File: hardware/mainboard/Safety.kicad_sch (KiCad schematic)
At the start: 19 parts, among them K1 IMB03ITS, Q6 2N7002, Q8 2N7002, Q9 2N7002, U3 74AUP1G32

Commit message: schematic?
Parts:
- removed C58: 100nF, Capacitor_SMD:C_0603_1608Metric, symbol Device:C_Small
- removed K1: IMB03ITS, Samacsys:IMB03ITS, symbol Samacsys_kicad_sym:IMB03ITS
- removed R15, R32, R41: 100, Resistor_SMD:R_0603_1608Metric, symbol Device:R_Small
- added K1: IM07DTS, Samacsys:IM23TS, symbol Samacsys_kicad_sym:IM07DTS
- added R38: 1k, Resistor_SMD:R_0603_1608Metric, symbol Device:R_Small
- added TP1, TP4: TestPoint_Small, TestPoint:TestPoint_Pad_D1.0mm, symbol Connector:TestPoint_Small
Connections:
- net AMS_OK is gone; now on net LED_ERR: Q9.1 (G), R13.1
- net WEB is gone; now on net WTDG_ERROR: Q8.1 (G)
- net GND: now also TP4.1
- net RELAY-: now also K1.8 (COIL_2)
- net SAFETY_IN: now also K1.3 (COM_1)
- net SAFETY_OUT: now also K1.4 (NO_1)
- net WTDG_ERROR: now also R38.1; no longer R14.2, U3.2
- net +3.3V renamed +3.3VIO
- net +5V renamed +24V
- net +24V: now also K1.1 (COIL_1)
- new net: R14.2, R38.2, TP1.1, U3.2
- no-connect marks 0 -> 4
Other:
- moved on the sheet: D7, Q8, Q9, R13, R14, TP17, TP18

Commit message: sync
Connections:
- net LED_ERR is gone; now on net WTDG_ERROR: Q8.3 (D), Q9.1 (G), R13.1
- net WTDG_ERROR: no longer Q8.1 (G), R38.1, U3.4
- new net LATCHERR: Q8.1 (G), R38.1, U3.4
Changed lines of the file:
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@@
 	(wire
 		(pts
-			(xy 125.73 133.35) (xy 147.32 133.35)
+			(xy 125.73 133.35) (xy 176.53 133.35)
 		)
 		(stroke
@@
 		)
 	)
+	(wire
+		(pts
+			(xy 176.53 133.35) (xy 176.53 82.55)
+		)
+		(stroke
+			(width 0)
+			(type default)
+		)
+	)
 	(polyline
 		(pts
@@
 	(wire
 		(pts
-			(xy 91.44 82.55) (xy 93.98 82.55)
+			(xy 91.44 82.55) (xy 176.53 82.55)
 		)
 		(stroke
@@
 			(width 0)
 			(type default)
+		)
+	)
+	(label "LATCHERR"
+		(at 127 133.35 0)
+		(effects
+			(font
+				(size 0.508 0.508)
+			)
+			(justify left bottom)
 		)
 	)
@@
 		)
 	)
-	(hierarchical_label "WTDG_ERROR"
-		(shape output)
-		(at 147.32 133.35 0)
+	(hierarchical_label "SAFETY_IN"
+		(shape bidirectional)
+		(at 118.11 45.72 0)
 		(effects
 			(font
@@
 		)
 	)
-	(hierarchical_label "LED_ERR"
-		(shape input)
-		(at 86.36 72.39 0)
-		(effects
-			(font
-				(size 1.27 1.27)
-			)
-			(justify left)
-		)
-	)
-	(hierarchical_label "SAFETY_IN"
-		(shape bidirectional)
-		(at 118.11 45.72 0)
-		(effects
-			(font
-				(size 1.27 1.27)
-			)
-			(justify left)
-		)
-	)
 	(hierarchical_label "AMS_ERROR"
 		(shape input)
@@
 	(hierarchical_label "WTDG_ERROR"
 		(shape output)
-		(at 93.98 82.55 0)
-		(effects
-			(font
+		(at 86.36 72.39 0)
+		(effects
+			(font

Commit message: hardware routing done, only touch ups will be needed if the board is aproved
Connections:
- net +3.3VIO renamed +5VIO
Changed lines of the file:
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@@
 	)
 	(symbol
-		(lib_id "power:+3.3V")
+		(lib_name "+5V_2")
+		(lib_id "power:+5V")
 		(at 99.06 67.31 270)
 		(unit 1)
@@
 		(on_board yes)
 		(dnp no)
-		(property "Reference" "#PWR059"
+		(property "Reference" "#PWR0119"
 			(at 95.25 67.31 0)
 			(effects
@@
 			)
 		)
-		(property "Value" "+3.3VIO"
+		(property "Value" "+5VIO"
 			(at 105.41 67.31 90)
 			(effects
@@
 			(project "PUTM_EV_AMS_MASTER_2025"
 				(path "/b456cffc-d9d7-4c91-91f2-36ec9a65dd1b/6eb4a2b1-8e5b-451b-b593-8aaaa3a4213e"
-					(reference "#PWR059")
+					(reference "#PWR0119")
 					(unit 1)
 				)
@@
 	)
 	(symbol
-		(lib_id "power:+3.3V")
-		(at 118.11 119.38 0)
-		(unit 1)
-		(exclude_from_sim no)
-		(in_bom yes)
-		(on_board yes)
-		(dnp no)
-		(property "Reference" "#PWR039"
-			(at 118.11 123.19 0)
-			(effects
-				(font
-					(size 1.27 1.27)
-				)
-				(hide yes)
-			)
-		)
-		(property "Value" "+3.3VIO"
-			(at 118.491 114.9858 0)
-			(effects
-				(font
-					(size 1.27 1.27)
-				)
-			)
-		)
-		(property "Footprint" ""
-			(at 118.11 119.38 0)
-			(effects
-				(font
-					(size 1.27 1.27)
-				)
-				(hide yes)
-			)
-		)
-		(property "Datasheet" ""
-			(at 118.11 119.38 0)
-			(effects
-				(font
-					(size 1.27 1.27)
-				)
-				(hide yes)
-			)
-		)
-		(property "Description" ""
-			(at 118.11 119.38 0)
-			(effects
-				(font
-					(size 1.27 1.27)
-				)
-				(hide yes)
-			)
-		)
-		(pin "1"
-		)
-		(instances
-			(project "PUTM_EV_BMS_HV_MASTER_2023"
-				(path "/b456cffc-d9d7-4c91-91f2-36ec9a65dd1b/6eb4a2b1-8e5b-451b-b593-8aaaa3a4213e"
-					(reference "#PWR039")
-					(unit 1)
-				)
-			)
-		)
-	)
-	(symbol
 		(lib_id "Device:R_Small")
 		(at 105.41 146.05 180)
@@
 	)
 	(symbol
-		(lib_id "power:+3.3V")
+		(lib_name "+5V_2")
+		(lib_id "power:+5V")
 		(at 74.93 121.92 0)
 		(unit 1)
@@
 		(on_board yes)
 		(dnp no)
-		(property "Reference" "#PWR044"
+		(property "Reference" "#PWR0121"
 			(at 74.93 125.73 0)
 			(effects
@@
 			)
 		)
-		(property "Value" "+3.3VIO"
-			(at 75.311 117.5258 0)
+		(property "Value" "+5VIO"
+			(at 74.93 118.11 0)
 			(effects
 				(font
@@
 		)
 		(instances
-			(project "PUTM_EV_BMS_HV_MASTER_2023"
+			(project "PUTM_EV_AMS_MASTER_2025"
 				(path "/b456cffc-d9d7-4c91-91f2-36ec9a65dd1b/6eb4a2b1-8e5b-451b-b593-8aaaa3a4213e"
-					(reference "#PWR044")
+					(reference "#PWR0121")
 					(unit 1)
 				)
+			)
+		)
+	)
+	(symbol
+		(lib_name "+5V_2")
+		(lib_id "power:+5V")
+		(at 118.11 119.38 0)
+		(unit 1)
+		(exclude_from_sim no)
+		(in_bom yes)
+		(on_board yes)
+		(dnp no)
+		(property "Reference" "#PWR0120"
+			(at 118.11 123.19 0)
+			(effects
+				(font
+					(size 1.27 1.27)
+				)
+				(hide yes)
+			)
+		)
+		(property "Value" "+5VIO"
+			(at 118.11 115.57 0)
+			(effects
+				(font
+					(size 1.27 1.27)
+				)
+			)
+		)
+		(property "Footprint" ""
+			(at 118.11 119.38 0)
+			(effects
+				(font
+					(size 1.27 1.27)
+				)
+				(hide yes)
+			)
+		)
+		(property "Datasheet" ""
+			(at 118.11 119.38 0)
+			(effects
+				(font
+					(size 1.27 1.27)
+				)
+				(hide yes)
+			)
+		)
+		(property "Description" ""
+			(at 118.11 119.38 0)
+			(effects
+				(font
+					(size 1.27 1.27)
+				)
+				(hide yes)
+			)
+		)
+		(pin "1"
+		)
+		(instances
+			(project "PUTM_EV_AMS_MASTER_2025"
+				(path "/b456cffc-d9d7-4c91-91f2-36ec9a65dd1b/6eb4a2b1-8e5b-451b-b593-8aaaa3a4213e"
+					(reference "#PWR0120")
+					(unit 1)
+				)

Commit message: isolation with every thing
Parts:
- removed D7: 60V/0.5/3A, Diode_SMD:D_SOD-123, symbol Device:D_Schottky_Small
- removed K1: IM07DTS, Samacsys:IM23TS, symbol Samacsys_kicad_sym:IM07DTS
- removed TP17, TP18: TestPoint_Small, TestPoint:TestPoint_THTPad_D1.0mm_Drill0.5mm, symbol Connector:TestPoint_Small
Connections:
- net RELAY- renamed ERROR_RELAY-
- no-connect marks 4 -> 0

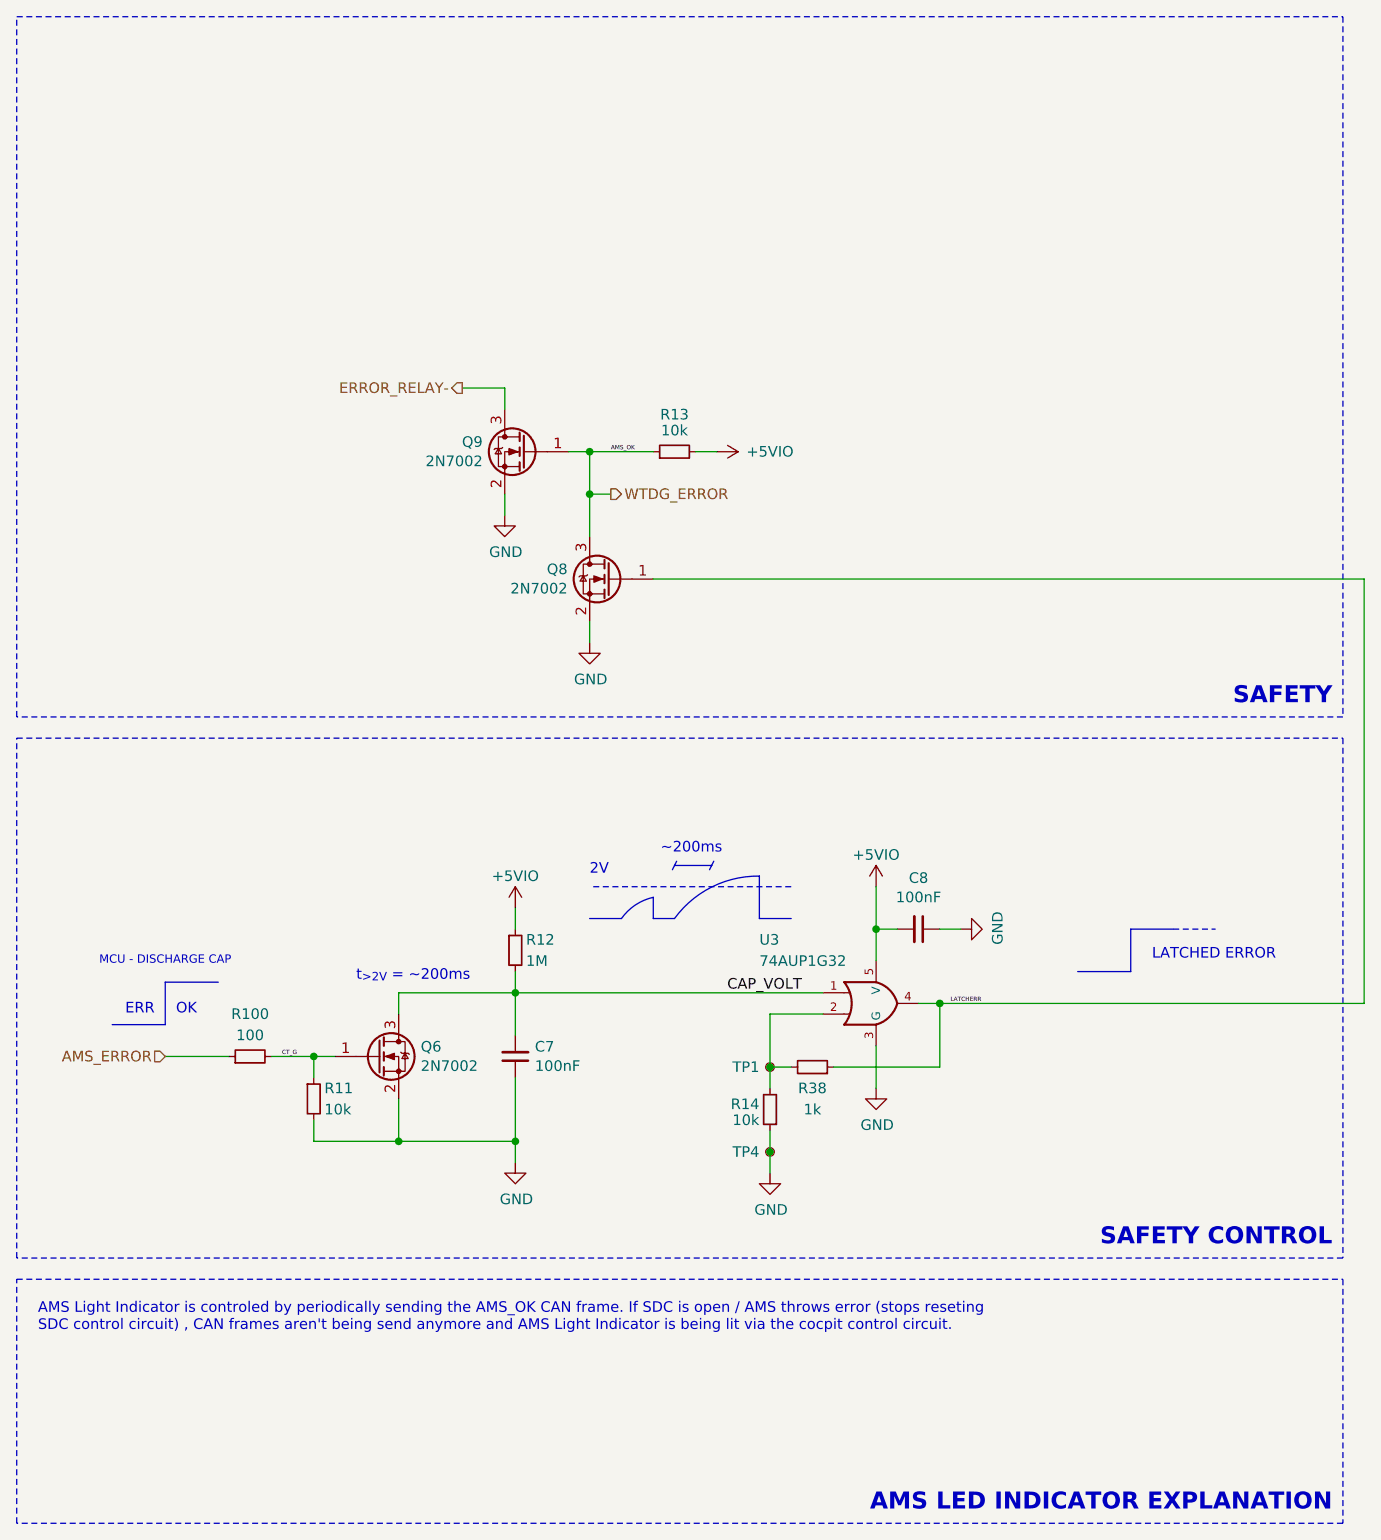
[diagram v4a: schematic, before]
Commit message: Cleaned up schematic, changed USB to UART, changed pinout of AIR sandwich connector
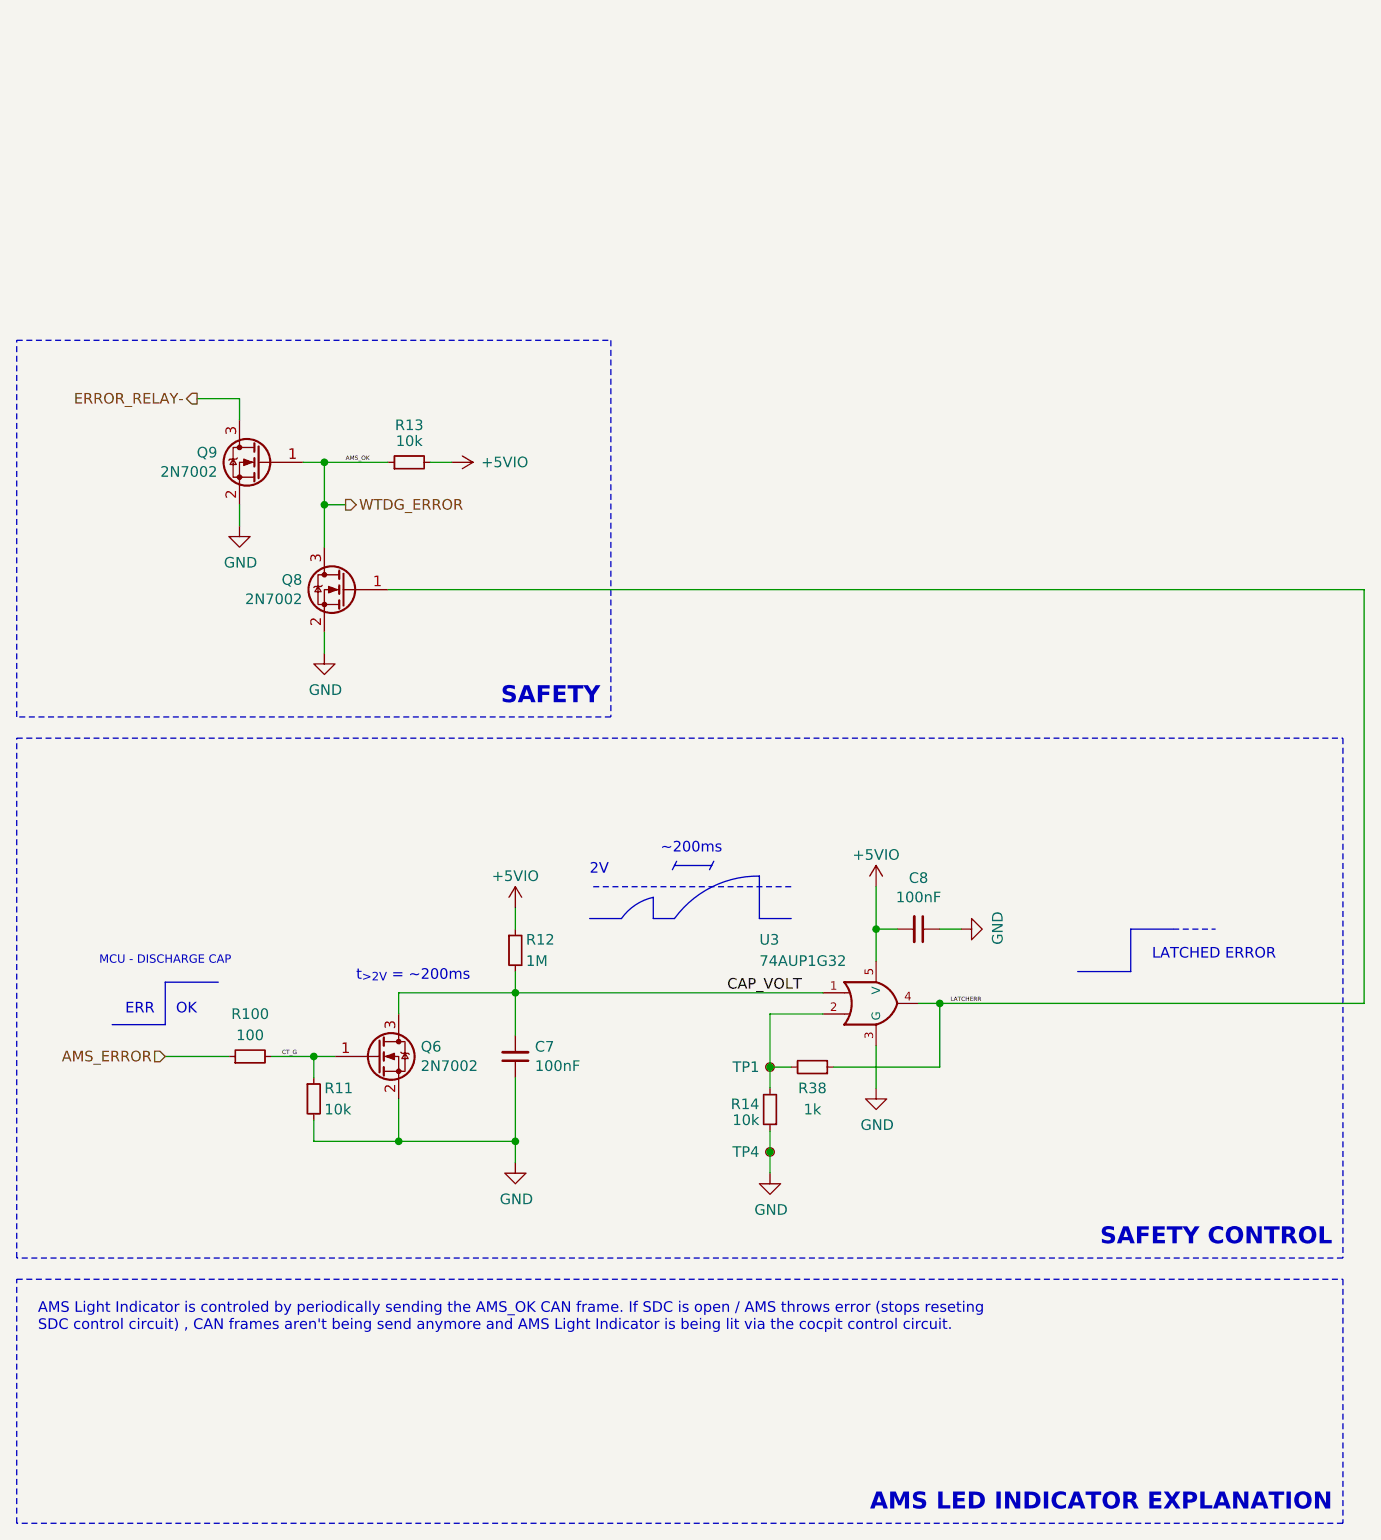
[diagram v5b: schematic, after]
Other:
- moved on the sheet: Q8, Q9, R13

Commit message: Layout again
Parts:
- added TP5, TP6, TP7: TestPoint_Small, TestPoint:TestPoint_Pad_D1.0mm, symbol Connector:TestPoint_Small
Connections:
- net CAP_VOLT: now also TP5.1
- net LATCHERR: now also TP6.1
- net WTDG_ERROR: now also TP7.1

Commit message: Plytka chyba fajnie zrobiona oprocz teardropow bo kicad 10 jest dziwny
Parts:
- TP5: value TestPoint_Small -> CAP_VOLT
- TP6: value TestPoint_Small -> LATCHED_ERR
- TP7: value TestPoint_Small -> WTDG_ERROR
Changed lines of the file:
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@@
+	(wire
+		(pts
+			(xy 64.77 68.58) (xy 67.31 68.58)
+		)
+		(stroke
+			(width 0)
+			(type default)
+		)
+	)
+	(wire
+		(pts
+			(xy 74.93 142.24) (xy 74.93 149.86)
+		)
+		(stroke
+			(width 0)
+			(type default)
+		)
+	)
+	(polyline
+		(pts
+			(xy 39.37 130.81) (xy 33.02 130.81)
+		)
+		(stroke
+			(width 0)
+			(type default)
+			(color 132 0 132 1)
+		)
+	)
+	(wire
+		(pts
+			(xy 52.07 66.04) (xy 52.07 68.58)
+		)
+		(stroke
+			(width 0)
+			(type default)
+		)
+	)
+	(polyline
+		(pts
+			(xy 104.14 123.19) (xy 104.14 118.11)
+		)
+		(stroke
+			(width 0)
+			(type default)
+			(color 132 0 132 1)
+		)
+	)
+	(polyline
+		(pts
+			(xy 26.67 135.89) (xy 33.02 135.89)
+		)
+		(stroke
+			(width 0)
+			(type default)
+			(color 132 0 132 1)
+		)
+	)
+	(polyline
+		(pts
+			(xy 91.44 123.19) (xy 91.44 120.65)
+		)
+		(stroke
+			(width 0)
+			(type default)
+			(color 132 0 132 1)
+		)
+	)
+	(wire
+		(pts
+			(xy 176.53 133.35) (xy 176.53 83.82)
+		)
+		(stroke
+			(width 0)
+			(type default)
+		)
+	)
+	(polyline
+		(pts
+			(xy 93.726 117.348) (xy 93.98 116.84)
+		)
+		(stroke
+			(width 0)
+			(type default)
+			(color 132 0 132 1)
+		)
+	)
+	(wire
+		(pts
+			(xy 123.19 133.35) (xy 125.73 133.35)
+		)
+		(stroke
+			(width 0)
+			(type default)
+		)
+	)
+	(wire
+		(pts
+			(xy 52.07 73.66) (xy 54.61 73.66)
+		)
+		(stroke
+			(width 0)
+			(type default)
+		)
+	)
+	(wire
+		(pts
+			(xy 41.91 73.66) (xy 41.91 76.2)
+		)
+		(stroke
+			(width 0)
+			(type default)
+		)
+	)
+	(polyline
+		(pts
+			(xy 91.44 123.19) (xy 93.98 123.19)
+		)
+		(stroke
+			(width 0)
+			(type default)
+			(color 132 0 132 1)
+		)
+	)
+	(wire
+		(pts
+			(xy 50.8 149.86) (xy 60.96 149.86)
+		)
+		(stroke
+			(width 0)
+			(type default)
+		)
+	)
+	(wire
+		(pts
+			(xy 74.93 129.54) (xy 74.93 132.08)
+		)
+		(stroke
+			(width 0)
+			(type default)
+		)
+	)
+	(wire
+		(pts
+			(xy 59.69 83.82) (xy 69.85 83.82)
+		)
+		(stroke
+			(width 0)
+			(type default)
+		)
+	)
+	(wire
+		(pts
+			(xy 69.85 83.82) (xy 176.53 83.82)
+		)
+		(stroke
+			(width 0)
+			(type default)
+		)
+	)
+	(wire
+		(pts
+			(xy 50.8 139.7) (xy 50.8 142.24)
+		)
+		(stroke
+			(width 0)
+			(type default)
+		)
+	)
+	(polyline
+		(pts
+			(xy 33.02 130.81) (xy 33.02 135.89)
+		)
+		(stroke
+			(width 0)
+			(type default)
+			(color 132 0 132 1)
+		)
+	)
 	(wire
 		(pts
@@
 			(width 0)
 			(type default)
-		)
-	)
-	(wire
-		(pts
-			(xy 64.77 68.58) (xy 67.31 68.58)
-		)
-		(stroke
-			(width 0)
-			(type default)
-		)
-	)
-	(wire
-		(pts
-			(xy 74.93 142.24) (xy 74.93 149.86)
-		)
-		(stroke
-			(width 0)
-			(type default)
-		)
-	)
-	(polyline
-		(pts
-			(xy 39.37 130.81) (xy 33.02 130.81)
-		)
-		(stroke
-			(width 0)
-			(type default)
-			(color 132 0 132 1)
-		)
-	)
-	(wire
-		(pts
-			(xy 52.07 66.04) (xy 52.07 68.58)
-		)
-		(stroke
-			(width 0)
-			(type default)
-		)
-	)
-	(polyline
-		(pts
-			(xy 104.14 123.19) (xy 104.14 118.11)
-		)
-		(stroke
-			(width 0)
-			(type default)
-			(color 132 0 132 1)
-		)
-	)
-	(polyline
-		(pts
-			(xy 26.67 135.89) (xy 33.02 135.89)
-		)
-		(stroke
-			(width 0)
-			(type default)
-			(color 132 0 132 1)
-		)
-	)
-	(polyline
-		(pts
-			(xy 91.44 123.19) (xy 91.44 120.65)
-		)
-		(stroke
-			(width 0)
-			(type default)
-			(color 132 0 132 1)
-		)
-	)
-	(wire
-		(pts
-			(xy 176.53 133.35) (xy 176.53 83.82)
-		)
-		(stroke
-			(width 0)
-			(type default)
-		)
-	)
-	(polyline
-		(pts
-			(xy 93.726 117.348) (xy 93.98 116.84)
-		)
-		(stroke
-			(width 0)
-			(type default)
-			(color 132 0 132 1)
-		)
-	)
-	(wire
-		(pts
-			(xy 123.19 133.35) (xy 125.73 133.35)
-		)
-		(stroke
-			(width 0)
-			(type default)
-		)
-	)
-	(wire
-		(pts
-			(xy 52.07 73.66) (xy 54.61 73.66)
-		)
-		(stroke
-			(width 0)
-			(type default)
-		)
-	)
-	(wire
-		(pts
-			(xy 41.91 73.66) (xy 41.91 76.2)
-		)
-		(stroke
-			(width 0)
-			(type default)
-		)
-	)
-	(polyline
-		(pts
-			(xy 91.44 123.19) (xy 93.98 123.19)
-		)
-		(stroke
-			(width 0)
-			(type default)
-			(color 132 0 132 1)
-		)
-	)
-	(wire
-		(pts
-			(xy 50.8 149.86) (xy 60.96 149.86)
-		)
-		(stroke
-			(width 0)
-			(type default)
-		)
-	)
-	(wire
-		(pts
-			(xy 74.93 129.54) (xy 74.93 132.08)
-		)
-		(stroke
-			(width 0)
-			(type default)
-		)
-	)
-	(wire
-		(pts
-			(xy 59.69 83.82) (xy 69.85 83.82)
-		)
-		(stroke
-			(width 0)
-			(type default)
-		)
-	)
-	(wire
-		(pts
-			(xy 69.85 83.82) (xy 176.53 83.82)
-		)
-		(stroke
-			(width 0)
-			(type default)
-		)
-	)
-	(wire
-		(pts
-			(xy 50.8 139.7) (xy 50.8 142.24)
-		)
-		(stroke
-			(width 0)
-			(type default)
-		)
-	)
-	(polyline
-		(pts
-			(xy 33.02 130.81) (xy 33.02 135.89)
-		)
-		(stroke
-			(width 0)
-			(type default)
-			(color 132 0 132 1)
 		)
 	)
@@
 			)
 		)
-		(property "Value" "TestPoint_Small"
+		(property "Value" "CAP_VOLT"
 			(at 86.36 129.5399 0)
 			(show_name no)
@@
 			)
 		)
-		(property "Value" "TestPoint_Small"
+		(property "Value" "WTDG_ERROR"
 			(at 52.07 63.5 90)
 			(show_name no)
@@
 			)
 		)
-		(property "Value" "TestPoint_Small"
+		(property "Value" "LATCHED_ERR"
 			(at 71.12 82.5499 0)
 			(show_name no)
